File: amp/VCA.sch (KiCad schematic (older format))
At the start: 15 parts, among them Q1 DMMT5401, U2 LM13700, U5 TL074

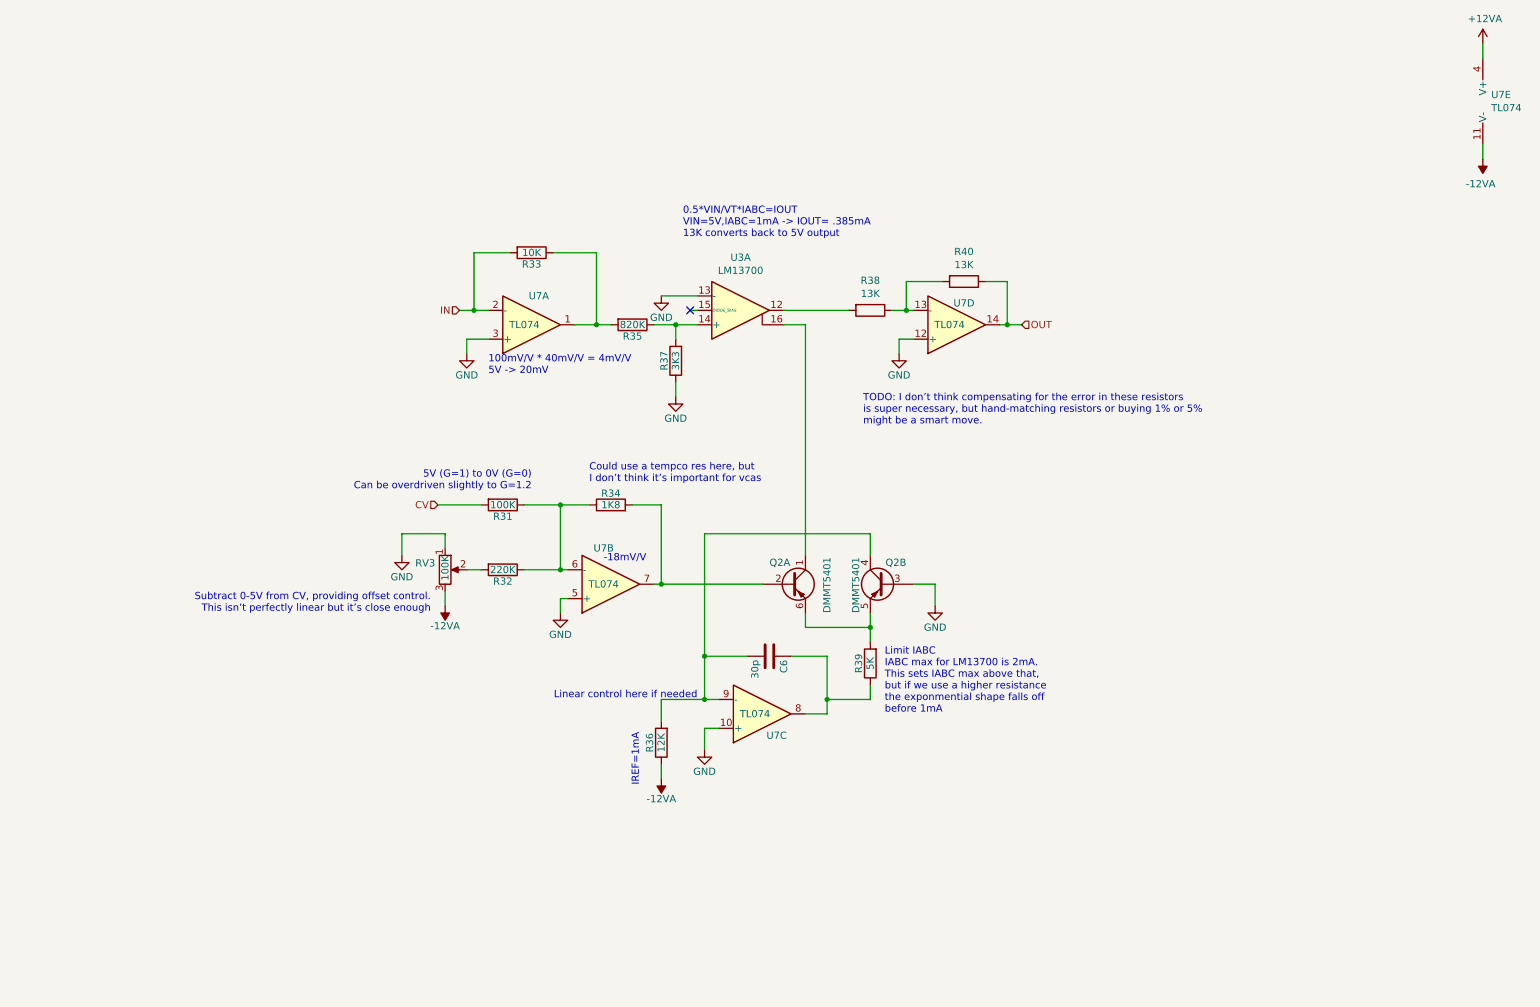
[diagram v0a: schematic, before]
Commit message: more vca layout
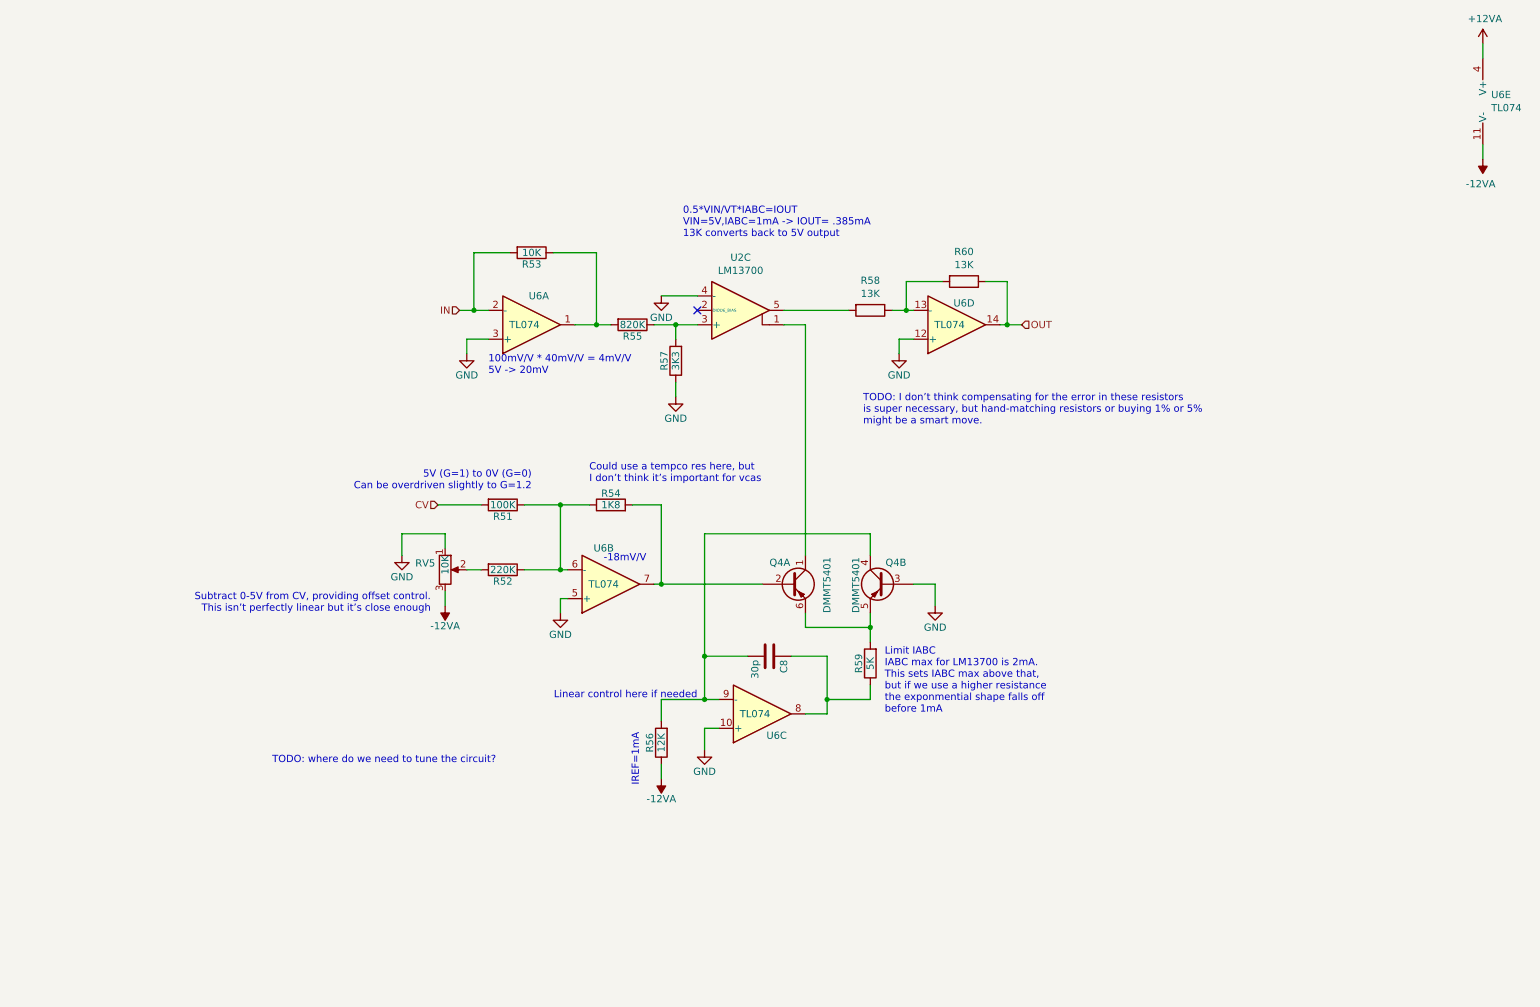
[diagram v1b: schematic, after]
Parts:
- RV2: value 100K -> 10K; footprint KiCad/kicad-footprints/Connector_PinHeader_2.54mm.pretty:PinHeader_1x03_P2.54mm_Vertical -> synth:slide_potentiometer_35mm
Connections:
- net GND: now also U2.4 (-); no longer U2.13 (-)
- net at Q1.1 (C1): now also U2.1; no longer U2.16
- net at R25.1, R27.2: now also U2.3 (+); no longer U2.14 (+)
- net at R28.2: now also U2.5; no longer U2.12
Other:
- note added: "TODO: where do we need to tune the circuit?"

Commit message: update amp
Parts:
- added R61: 100K, KiCad/Resistors_ThroughHole.pretty:R_Axial_DIN0204_L3.6mm_D1.6mm_P1.90mm_Vertical, symbol Device:R
- added RT1: 5K, symbol Device:RTRIM
- R26: value 12K -> 10K
- R27: value 3K3 -> 33K
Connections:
- net -12VA: now also RT1.2; no longer R26.1
- net GND: now also U2.13 (-); no longer U2.4 (-)
- net IN: now also R61.2; no longer R23.2, U5.2 (-)
- net at Q1.1 (C1): now also U2.16; no longer U2.1
- net at R25.1, R27.2: now also U2.14 (+); no longer U2.3 (+)
- net at R28.2: now also U2.12; no longer U2.5
- new net: R26.1, RT1.1
- new net: R23.2, R61.1, U5.2 (-)
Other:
- note added: "12K -> IREF=1mA\nTRIM compensates for component tolerance"
- note added: "TODO: order:\n820Ks\n13Ks (1%)"
- note removed: "IREF=1mA"
- note removed: "TODO: I don’t think compensating for the error in these resistors\nis super necessary, but hand-matching resistors or buying 1% or 5%\nmight be a smart move."
- note removed: "TODO: where do we need to tune the circuit?"
- moved on the sheet: R26

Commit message: updated schematic to match
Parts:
- removed R25: 820K, KiCad/Resistors_ThroughHole.pretty:R_Axial_DIN0204_L3.6mm_D1.6mm_P1.90mm_Vertical, symbol Device:R
- removed R27: 33K, KiCad/Resistors_ThroughHole.pretty:R_Axial_DIN0204_L3.6mm_D1.6mm_P1.90mm_Vertical, symbol Device:R
- added R22: 50K, symbol Device:RTRIM
- added R31: 10K, symbol Device:RTRIM
- R21: renamed from R61; value 100K -> 820K
- R23: renamed from R21; value 100K -> 120K
- R24: renamed from R22; value 220K -> 270K
- R25: renamed from R23; value 10K -> 3K3
- R26: renamed from R24; value 1K8 -> 3K3
- R27: renamed from R26; value 10K -> 22K
- R28: value 13K -> 27K
- R30: value 13K -> 22K
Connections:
- net OUT: now also R31.2; no longer R30.1
- net at R24.2: now also R22.1; no longer RV2.2
- net at R25.1, U5.1: now also U2.14 (+)
- new net: R22.2, RV2.2
- new net: R30.1, R31.1
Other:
- note added: "0.5*VIN/VT*IABC=IOUT\nVIN/VT=20mV/26mV,IABC=0.5mA -> IOUT= .192mA\n27K converts back to 5V output"
- note added: "5V (G=1) to 0V (G=about 0)\nCan be overdriven to G=2 @ 6V"
- note added: "Could use a tempco res here, but\nI don’t think temp dependance is\nimportant for vcas"
- note added: "Limit IABC to 2mA\nmax for LM13700"
- note added: "TODO: order:\n820Ks\ntrimmers"
- note added: "TUNE 1: calculated 288K\nadjust so CV=5V sets VB=0V"
- note added: "TUNE 2: calculated 24K\nadjust so current is 0.5mA @ VB=0"
- note added: "TUNE 3: calculated 27K\nadjust to 5V at g=1"
- note added: "gain=.004 => 4mV/V => 5V -> 20mV\n20mV is max linear input for LM13700\nwithout using diodes"
- note removed: "0.5*VIN/VT*IABC=IOUT\nVIN=5V,IABC=1mA -> IOUT= .385mA\n13K converts back to 5V output"
- note removed: "100mV/V * 40mV/V = 4mV/V\n5V -> 20mV"
- note removed: "12K -> IREF=1mA\nTRIM compensates for component tolerance"
- note removed: "5V (G=1) to 0V (G=0)\nCan be overdriven slightly to G=1.2"
- note removed: "Could use a tempco res here, but\nI don’t think it’s important for vcas"
- note removed: "Limit IABC\nIABC max for LM13700 is 2mA.\nThis sets IABC max above that,\nbut if we use a higher resistance\nthe exponmential shape falls off\nbefore 1mA"
- note removed: "TODO: order:\n820Ks\n13Ks (1%)"
- moved on the sheet: R28, R30, RV2

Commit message: documented utils
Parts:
- renumbered R23 to R22, R24 to R23, R25 to R24, R26 to R25, R27 to R26, R28 to R27, R29 to R28, R30 to R29, R22 to RT1, RT1 to RT2, R31 to RT3
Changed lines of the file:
@@
 $EndComp
 $Comp
-L Device:R R27
+L Device:R R26
 U 1 1 5EBBC2A7
 P 5100 5550
-AR Path="/5EBA9693/5EBBC2A7" Ref="R27"  Part="1"
+AR Path="/5EBA9693/5EBBC2A7" Ref="R26"  Part="1"
 AR Path="/5EE5C6CB/5EBBC2A7" Ref="R?"  Part="1"
-AR Path="/5EE915A8/5EBBC2A7" Ref="R60"  Part="1"
-AR Path="/5EE915EC/5EBBC2A7" Ref="R38"  Part="1"
-AR Path="/5EE9163B/5EBBC2A7" Ref="R49"  Part="1"
-F 0 "R27" V 5180 5550 50  0000 C CNN
+AR Path="/5EE915A8/5EBBC2A7" Ref="R53"  Part="1"
+AR Path="/5EE915EC/5EBBC2A7" Ref="R35"  Part="1"
+AR Path="/5EE9163B/5EBBC2A7" Ref="R44"  Part="1"
+F 0 "R26" V 5180 5550 50  0000 C CNN
 F 1 "22K" V 5100 5550 50  0000 C CNN
 F 2 "KiCad/Resistors_ThroughHole.pretty:R_Axial_DIN0204_L3.6mm_D1.6mm_P1.90mm_Vertical" V 5030 5550 50  0001 C CNN
@@
 Linear control here if needed
 $Comp
-L Device:R R29
+L Device:R R28
 U 1 1 5EBBC2B9
 P 6550 5050
-AR Path="/5EBA9693/5EBBC2B9" Ref="R29"  Part="1"
+AR Path="/5EBA9693/5EBBC2B9" Ref="R28"  Part="1"
 AR Path="/5EE5C6CB/5EBBC2B9" Ref="R?"  Part="1"
-AR Path="/5EE915A8/5EBBC2B9" Ref="R62"  Part="1"
-AR Path="/5EE915EC/5EBBC2B9" Ref="R40"  Part="1"
-AR Path="/5EE9163B/5EBBC2B9" Ref="R51"  Part="1"
-F 0 "R29" V 6630 5050 50  0000 C CNN
+AR Path="/5EE915A8/5EBBC2B9" Ref="R55"  Part="1"
+AR Path="/5EE915EC/5EBBC2B9" Ref="R37"  Part="1"
+AR Path="/5EE9163B/5EBBC2B9" Ref="R46"  Part="1"
+F 0 "R28" V 6630 5050 50  0000 C CNN
 F 1 "5K" V 6550 5050 50  0000 C CNN
 F 2 "KiCad/Resistors_ThroughHole.pretty:R_Axial_DIN0204_L3.6mm_D1.6mm_P1.90mm_Vertical" V 6480 5050 50  0001 C CNN
@@
 $EndComp
 $Comp
-L Device:R R26
+L Device:R R25
 U 1 1 5EBBC2CB
 P 4750 3950
-AR Path="/5EBA9693/5EBBC2CB" Ref="R26"  Part="1"
+AR Path="/5EBA9693/5EBBC2CB" Ref="R25"  Part="1"
 AR Path="/5EE5C6CB/5EBBC2CB" Ref="R?"  Part="1"
-AR Path="/5EE915A8/5EBBC2CB" Ref="R59"  Part="1"
-AR Path="/5EE915EC/5EBBC2CB" Ref="R37"  Part="1"
-AR Path="/5EE9163B/5EBBC2CB" Ref="R48"  Part="1"
-F 0 "R26" V 4830 3950 50  0000 C CNN
+AR Path="/5EE915A8/5EBBC2CB" Ref="R52"  Part="1"
+AR Path="/5EE915EC/5EBBC2CB" Ref="R34"  Part="1"
+AR Path="/5EE9163B/5EBBC2CB" Ref="R43"  Part="1"
+F 0 "R25" V 4830 3950 50  0000 C CNN
 F 1 "3K3" V 4750 3950 50  0000 C CNN
 F 2 "KiCad/Resistors_ThroughHole.pretty:R_Axial_DIN0204_L3.6mm_D1.6mm_P1.90mm_Vertical" V 4680 3950 50  0001 C CNN
@@
 $EndComp
 $Comp
-L Device:R R23
+L Device:R R22
 U 1 1 5EBBC2D7
 P 4000 3950
-AR Path="/5EBA9693/5EBBC2D7" Ref="R23"  Part="1"
+AR Path="/5EBA9693/5EBBC2D7" Ref="R22"  Part="1"
 AR Path="/5EE5C6CB/5EBBC2D7" Ref="R?"  Part="1"
-AR Path="/5EE915A8/5EBBC2D7" Ref="R56"  Part="1"
-AR Path="/5EE915EC/5EBBC2D7" Ref="R34"  Part="1"
-AR Path="/5EE9163B/5EBBC2D7" Ref="R45"  Part="1"
-F 0 "R23" V 4080 3950 50  0000 C CNN
+AR Path="/5EE915A8/5EBBC2D7" Ref="R49"  Part="1"
+AR Path="/5EE915EC/5EBBC2D7" Ref="R31"  Part="1"
+AR Path="/5EE9163B/5EBBC2D7" Ref="R40"  Part="1"
+F 0 "R22" V 4080 3950 50  0000 C CNN
 F 1 "120K" V 4000 3950 50  0000 C CNN
 F 2 "KiCad/Resistors_ThroughHole.pretty:R_Axial_DIN0204_L3.6mm_D1.6mm_P1.90mm_Vertical" V 3930 3950 50  0001 C CNN
@@
 $EndComp
 $Comp
-L Device:R R24
+L Device:R R23
 U 1 1 5EBBC2E3
 P 4000 4400
-AR Path="/5EBA9693/5EBBC2E3" Ref="R24"  Part="1"
+AR Path="/5EBA9693/5EBBC2E3" Ref="R23"  Part="1"
 AR Path="/5EE5C6CB/5EBBC2E3" Ref="R?"  Part="1"
-AR Path="/5EE915A8/5EBBC2E3" Ref="R57"  Part="1"
-AR Path="/5EE915EC/5EBBC2E3" Ref="R35"  Part="1"
-AR Path="/5EE9163B/5EBBC2E3" Ref="R46"  Part="1"
-F 0 "R24" V 4080 4400 50  0000 C CNN
+AR Path="/5EE915A8/5EBBC2E3" Ref="R50"  Part="1"
+AR Path="/5EE915EC/5EBBC2E3" Ref="R32"  Part="1"
+AR Path="/5EE9163B/5EBBC2E3" Ref="R41"  Part="1"
+F 0 "R23" V 4080 4400 50  0000 C CNN
 F 1 "270K" V 4000 4400 50  0000 C CNN
 F 2 "KiCad/Resistors_ThroughHole.pretty:R_Axial_DIN0204_L3.6mm_D1.6mm_P1.90mm_Vertical" V 3930 4400 50  0001 C CNN
@@
 	3750 2800 3900 2800
 $Comp
-L Device:R R25
+L Device:R R24
 U 1 1 5EBBC326
 P 4200 2200
-AR Path="/5EBA9693/5EBBC326" Ref="R25"  Part="1"
+AR Path="/5EBA9693/5EBBC326" Ref="R24"  Part="1"
 AR Path="/5EE5C6CB/5EBBC326" Ref="R?"  Part="1"
-AR Path="/5EE915A8/5EBBC326" Ref="R58"  Part="1"
-AR Path="/5EE915EC/5EBBC326" Ref="R36"  Part="1"
-AR Path="/5EE9163B/5EBBC326" Ref="R47"  Part="1"
-F 0 "R25" V 4280 2200 50  0000 C CNN
+AR Path="/5EE915A8/5EBBC326" Ref="R51"  Part="1"
+AR Path="/5EE915EC/5EBBC326" Ref="R33"  Part="1"
+AR Path="/5EE9163B/5EBBC326" Ref="R42"  Part="1"
+F 0 "R24" V 4280 2200 50  0000 C CNN
 F 1 "3K3" V 4200 2200 50  0000 C CNN
 F 2 "KiCad/Resistors_ThroughHole.pretty:R_Axial_DIN0204_L3.6mm_D1.6mm_P1.90mm_Vertical" V 4130 2200 50  0001 C CNN
@@
 NoConn ~ 5350 2600
 $Comp
-L Device:R R28
+L Device:R R27
 U 1 1 5F07C242
 P 6450 2600
-AR Path="/5EBA9693/5F07C242" Ref="R28"  Part="1"
-AR Path="/5EE915EC/5F07C242" Ref="R39"  Part="1"
-AR Path="/5EE9163B/5F07C242" Ref="R50"  Part="1"
-AR Path="/5EE915A8/5F07C242" Ref="R61"  Part="1"
-F 0 "R28" V 6350 2600 50  0000 C CNN
+AR Path="/5EBA9693/5F07C242" Ref="R27"  Part="1"
+AR Path="/5EE915EC/5F07C242" Ref="R36"  Part="1"
+AR Path="/5EE9163B/5F07C242" Ref="R45"  Part="1"
+AR Path="/5EE915A8/5F07C242" Ref="R54"  Part="1"
+F 0 "R27" V 6350 2600 50  0000 C CNN
 F 1 "27K" V 6450 2600 50  0000 C CNN
 F 2 "KiCad/Resistors_ThroughHole.pretty:R_Axial_DIN0204_L3.6mm_D1.6mm_P1.90mm_Vertical" V 6380 2600 50  0001 C CNN
@@
 	6750 2800 6850 2800
 $Comp
-L Device:R R30
+L Device:R R29
 U 1 1 5F083AFD
 P 7000 2400
-AR Path="/5EBA9693/5F083AFD" Ref="R30"  Part="1"
-AR Path="/5EE915EC/5F083AFD" Ref="R41"  Part="1"
-AR Path="/5EE9163B/5F083AFD" Ref="R52"  Part="1"
-AR Path="/5EE915A8/5F083AFD" Ref="R63"  Part="1"
-F 0 "R30" V 6900 2400 50  0000 C CNN
+AR Path="/5EBA9693/5F083AFD" Ref="R29"  Part="1"
+AR Path="/5EE915EC/5F083AFD" Ref="R38"  Part="1"
+AR Path="/5EE9163B/5F083AFD" Ref="R47"  Part="1"
+AR Path="/5EE915A8/5F083AFD" Ref="R56"  Part="1"
+F 0 "R29" V 6900 2400 50  0000 C CNN
 F 1 "22K" V 7000 2400 50  0000 C CNN
 F 2 "KiCad/Resistors_ThroughHole.pretty:R_Axial_DIN0204_L3.6mm_D1.6mm_P1.90mm_Vertical" V 6930 2400 50  0001 C CNN
@@
 AR Path="/5EBA9693/5EE2FBCC" Ref="R21"  Part="1"
 AR Path="/5EE5C6CB/5EE2FBCC" Ref="R?"  Part="1"
-AR Path="/5EE915A8/5EE2FBCC" Ref="R54"  Part="1"
-AR Path="/5EE915EC/5EE2FBCC" Ref="R32"  Part="1"
-AR Path="/5EE9163B/5EE2FBCC" Ref="R43"  Part="1"
+AR Path="/5EE915A8/5EE2FBCC" Ref="R48"  Part="1"
+AR Path="/5EE915EC/5EE2FBCC" Ref="R30"  Part="1"
+AR Path="/5EE9163B/5EE2FBCC" Ref="R39"  Part="1"
 F 0 "R21" V 3630 2600 50  0000 C CNN
 F 1 "820K" V 3550 2600 50  0000 C CNN
@@
 Could use a tempco res here, but\nI don’t think temp dependance is\nimportant for vcas
 $Comp
-L Device:RTRIM RT1
+L Device:RTRIM RT2
 U 1 1 5EE41C5F
 P 5100 5950
-AR Path="/5EBA9693/5EE41C5F" Ref="RT1"  Part="1"
-AR Path="/5EE915A8/5EE41C5F" Ref="RT4"  Part="1"
-AR Path="/5EE915EC/5EE41C5F" Ref="RT2"  Part="1"
-AR Path="/5EE9163B/5EE41C5F" Ref="RT3"  Part="1"
-F 0 "RT1" H 5200 6000 50  0000 L CNN
+AR Path="/5EBA9693/5EE41C5F" Ref="RT2"  Part="1"
+AR Path="/5EE915A8/5EE41C5F" Ref="RT11"  Part="1"
+AR Path="/5EE915EC/5EE41C5F" Ref="RT5"  Part="1"
+AR Path="/5EE9163B/5EE41C5F" Ref="RT8"  Part="1"
+F 0 "RT2" H 5200 6000 50  0000 L CNN
 F 1 "5K" H 5200 5900 50  0000 L CNN
 F 2 "" V 5030 5950 50  0001 C CNN
@@
 TUNE 3: calculated 27K\nadjust to 5V at g=1
 $Comp
-L Device:RTRIM R22
+L Device:RTRIM RT1
 U 1 1 5EDE0DC3
 P 3600 4400
-AR Path="/5EBA9693/5EDE0DC3" Ref="R22"  Part="1"
-AR Path="/5EE915EC/5EDE0DC3" Ref="R33"  Part="1"
-AR Path="/5EE9163B/5EDE0DC3" Ref="R44"  Part="1"
-AR Path="/5EE915A8/5EDE0DC3" Ref="R55"  Part="1"
-F 0 "R22" V 3360 4400 50  0000 C CNN
+AR Path="/5EBA9693/5EDE0DC3" Ref="RT1"  Part="1"
+AR Path="/5EE915EC/5EDE0DC3" Ref="RT4"  Part="1"
+AR Path="/5EE9163B/5EDE0DC3" Ref="RT7"  Part="1"
+AR Path="/5EE915A8/5EDE0DC3" Ref="RT10"  Part="1"
+F 0 "RT1" V 3360 4400 50  0000 C CNN
 F 1 "50K" V 3451 4400 50  0000 C CNN
 F 2 "" V 3530 4400 50  0001 C CNN
@@
 	4650 2700 5350 2700
 $Comp
-L Device:RTRIM R31
+L Device:RTRIM RT3
 U 1 1 5EDF3544
 P 7350 2400
-AR Path="/5EBA9693/5EDF3544" Ref="R31"  Part="1"
-AR Path="/5EE915EC/5EDF3544" Ref="R42"  Part="1"
-AR Path="/5EE9163B/5EDF3544" Ref="R53"  Part="1"
-AR Path="/5EE915A8/5EDF3544" Ref="R64"  Part="1"
-F 0 "R31" V 7615 2400 50  0000 C CNN
+AR Path="/5EBA9693/5EDF3544" Ref="RT3"  Part="1"
+AR Path="/5EE915EC/5EDF3544" Ref="RT6"  Part="1"
+AR Path="/5EE9163B/5EDF3544" Ref="RT9"  Part="1"
+AR Path="/5EE915A8/5EDF3544" Ref="RT12"  Part="1"
+F 0 "RT3" V 7615 2400 50  0000 C CNN
 F 1 "10K" V 7524 2400 50  0000 C CNN
 F 2 "" V 7280 2400 50  0001 C CNN
